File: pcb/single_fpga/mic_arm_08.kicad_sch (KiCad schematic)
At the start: 17 parts, among them U107 CDCLVC1108PW, U65 IM72D128V01XTMA1, U66 IM72D128V01XTMA1, U67 IM72D128V01XTMA1, U68 IM72D128V01XTMA1, U69 IM72D128V01XTMA1, U70 IM72D128V01XTMA1, U71 IM72D128V01XTMA1, U72 IM72D128V01XTMA1

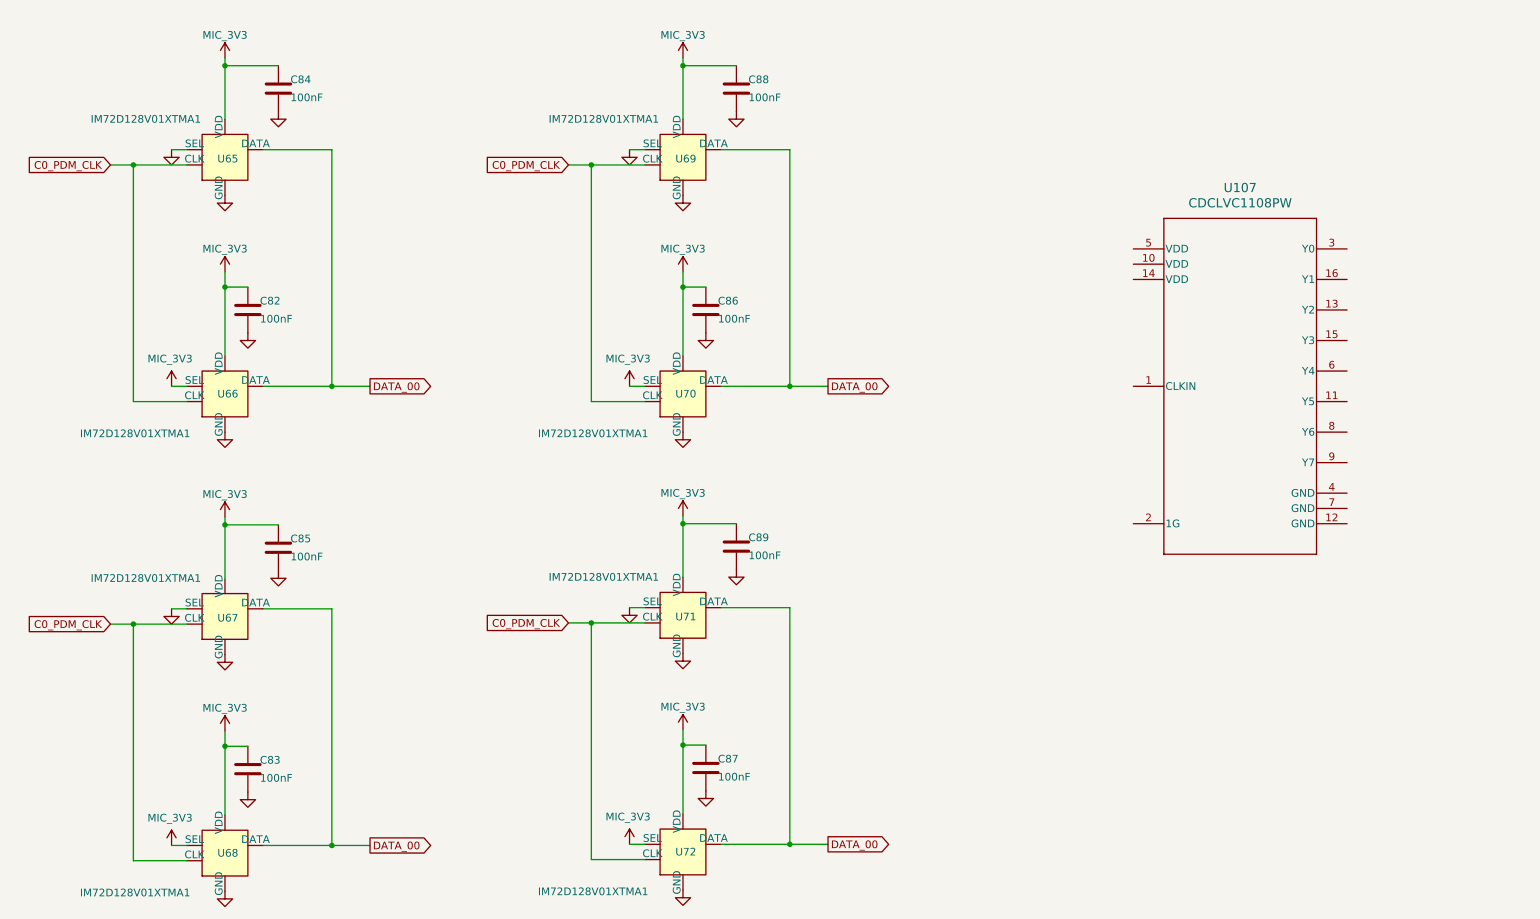
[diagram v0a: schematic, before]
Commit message: Fixed clocks and names.
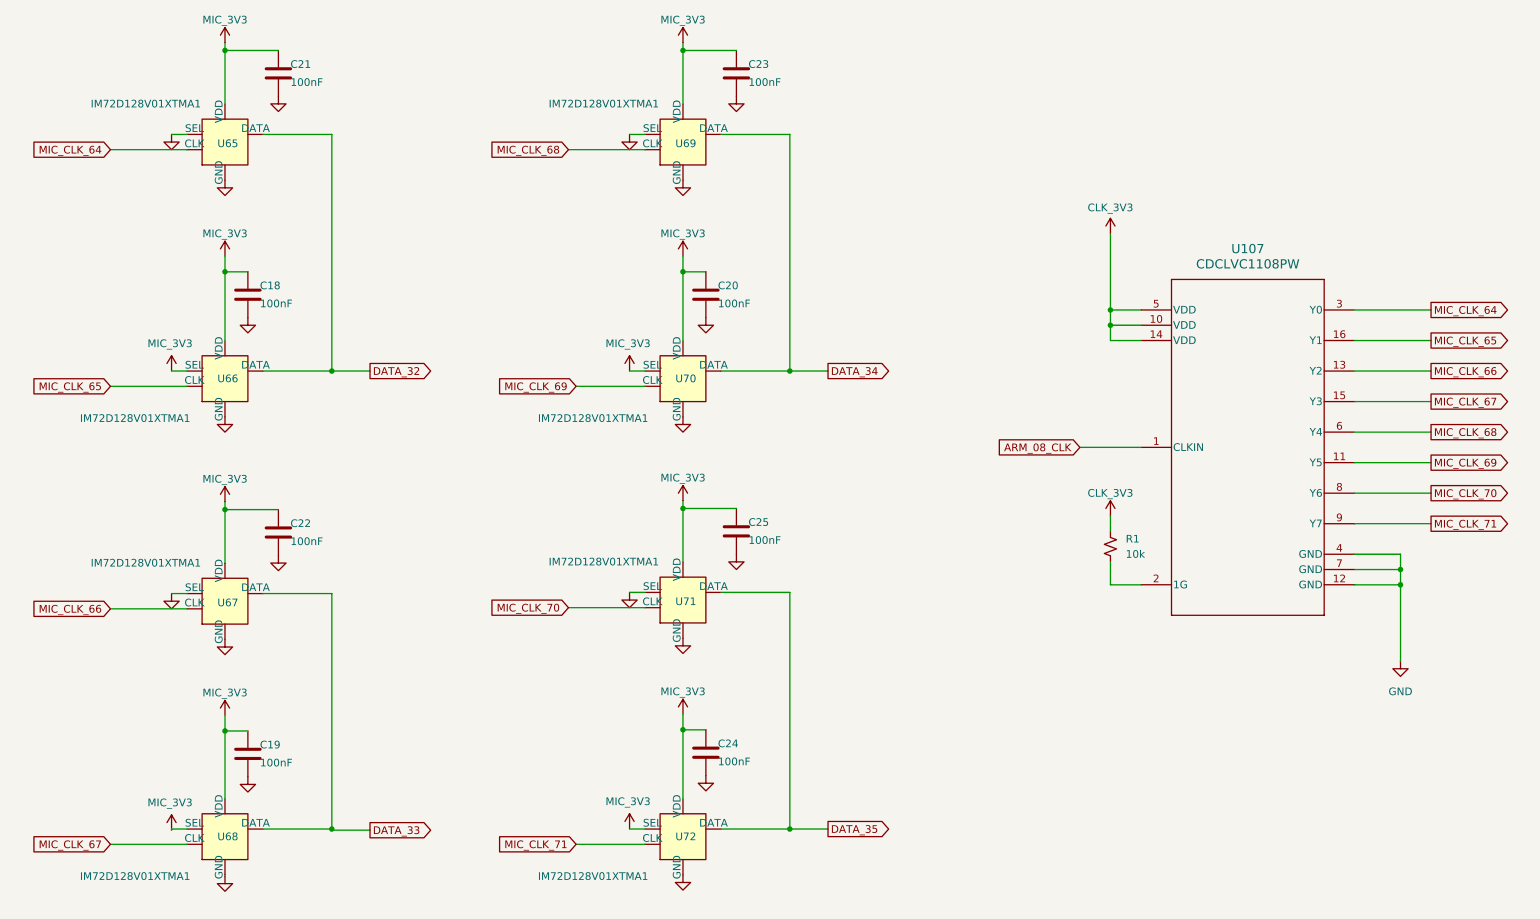
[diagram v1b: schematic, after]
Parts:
- removed C82, C83, C84, C85, C86, C87, C88, C89: 100nF, Capacitor_SMD:C_0603_1608Metric, symbol Device:C
- added C18, C19, C20, C21, C22, C23, C24, C25: 100nF, Capacitor_SMD:C_0603_1608Metric, symbol Device:C
- added R1: 10k, PCM_SparkFun-Resistor:R_0603_1608Metric, symbol PCM_SparkFun-Resistor:10k_0603
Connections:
- net GND: now also U107.12 (GND), U107.4 (GND), U107.7 (GND), C18.2, C19.2, C20.2, C21.2, C22.2, C23.2, C24.2, C25.2
- net MIC_3V3: now also C18.1, C19.1, C20.1, C21.1, C22.1, C23.1, C24.1, C25.1
- net ARM_08_CLK: now reaches U107.1 (CLKIN)
- net CLK_3V3: now reaches U107.10 (VDD)
- net CLK_3V3: now also U107.14 (VDD), U107.5 (VDD), R1.2
- net MIC_CLK_69: now reaches U107.11 (Y5)
- net MIC_CLK_69: now also U70.3 (CLK)
- net MIC_CLK_66: now reaches U107.13 (Y2)
- net MIC_CLK_66: now also U67.3 (CLK)
- net MIC_CLK_67: now reaches U107.15 (Y3)
- net MIC_CLK_67: now also U68.3 (CLK)
- net MIC_CLK_65: now reaches U107.16 (Y1)
- net MIC_CLK_65: now also U66.3 (CLK)
- net at U107.2 (1G): now also R1.1
- net MIC_CLK_64: now reaches U107.3 (Y0)
- net MIC_CLK_64: now also U65.3 (CLK)
- net MIC_CLK_68: now reaches U107.6 (Y4)
- net MIC_CLK_68: now also U69.3 (CLK)
- net MIC_CLK_70: now reaches U107.8 (Y6)
- net MIC_CLK_70: now also U71.3 (CLK)
- net MIC_CLK_71: now reaches U107.9 (Y7)
- net MIC_CLK_71: now also U72.3 (CLK)
- removed net C0_PDM_CLK: U65.3 (CLK), U66.3 (CLK), U67.3 (CLK), U68.3 (CLK), U69.3 (CLK), U70.3 (CLK), U71.3 (CLK), U72.3 (CLK)
- removed net DATA_00: U65.1 (DATA), U66.1 (DATA), U67.1 (DATA), U68.1 (DATA), U69.1 (DATA), U70.1 (DATA), U71.1 (DATA), U72.1 (DATA)
- new net DATA_32: U65.1 (DATA), U66.1 (DATA)
- new net DATA_33: U67.1 (DATA), U68.1 (DATA)
- new net DATA_34: U69.1 (DATA), U70.1 (DATA)
- new net DATA_35: U71.1 (DATA), U72.1 (DATA)

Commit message: Fixed all duplicate refdes's.
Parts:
- renumbered C18 to C82, C19 to C83, C20 to C84, C21 to C85, C22 to C86, C23 to C87, C24 to C88, C25 to C89, R1 to R13

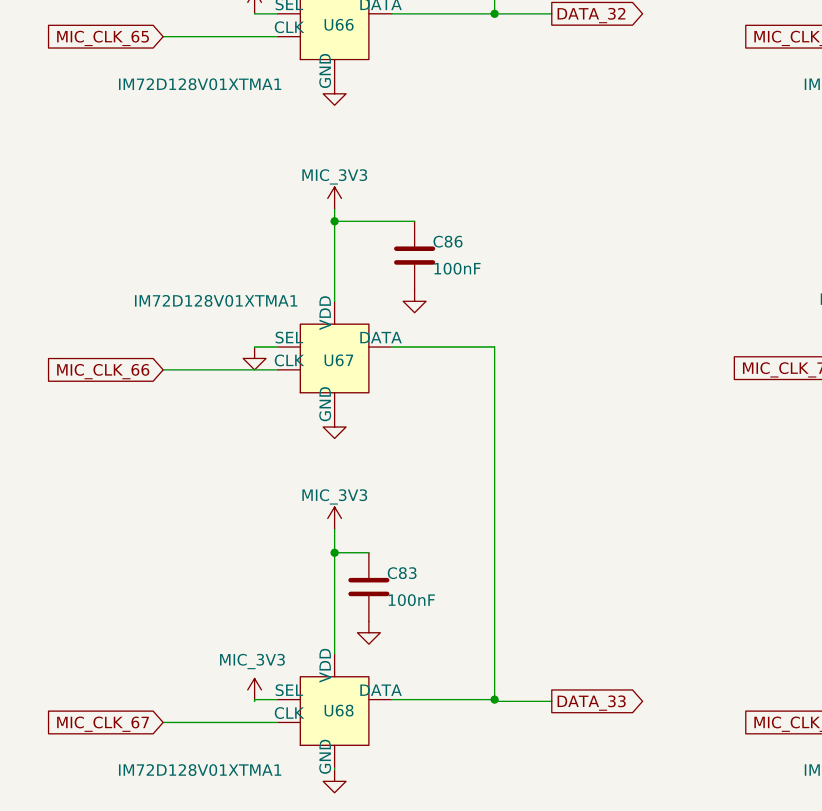
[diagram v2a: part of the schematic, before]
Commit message: Fixed symbol library references.
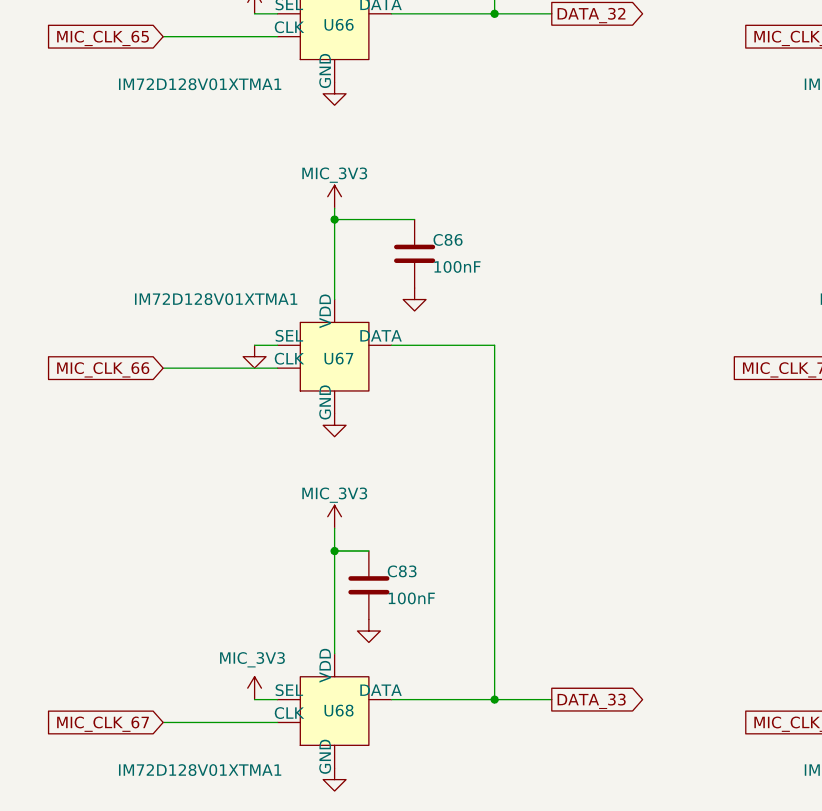
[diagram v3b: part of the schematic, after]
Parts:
- U107: footprint PW0016A_N -> CDCLVC1108:PW0016A_N

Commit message: Fixed footprints. Added missing mic. Relinked placed footprints.
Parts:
- U65, U66, U67, U68, U69, U70, U71, U72: footprint (none) -> IM72D128:IFX-PG-LLGA-5-4
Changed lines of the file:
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@@
 			)
 		)
-		(property "Footprint" ""
+		(property "Footprint" "IM72D128:IFX-PG-LLGA-5-4"
 			(at 59.69 160.02 0)
 			(hide yes)
@@
 			)
 		)
-		(property "Footprint" ""
+		(property "Footprint" "IM72D128:IFX-PG-LLGA-5-4"
 			(at 135.89 160.02 0)
 			(hide yes)
@@
 			)
 		)
-		(property "Footprint" ""
+		(property "Footprint" "IM72D128:IFX-PG-LLGA-5-4"
 			(at 59.69 83.82 0)
 			(hide yes)
@@
 			)
 		)
-		(property "Footprint" ""
+		(property "Footprint" "IM72D128:IFX-PG-LLGA-5-4"
 			(at 59.69 120.65 0)
 			(hide yes)
@@
 			)
 		)
-		(property "Footprint" ""
+		(property "Footprint" "IM72D128:IFX-PG-LLGA-5-4"
 			(at 59.69 44.45 0)
 			(hide yes)
@@
 			)
 		)
-		(property "Footprint" ""
+		(property "Footprint" "IM72D128:IFX-PG-LLGA-5-4"
 			(at 135.89 83.82 0)
 			(hide yes)
@@
 			)
 		)
-		(property "Footprint" ""
+		(property "Footprint" "IM72D128:IFX-PG-LLGA-5-4"
 			(at 135.89 44.45 0)
 			(hide yes)
@@
 			)
 		)
-		(property "Footprint" ""
+		(property "Footprint" "IM72D128:IFX-PG-LLGA-5-4"
 			(at 135.89 120.65 0)
 			(hide yes)

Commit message: Updated all refdes's.
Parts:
- removed C82, C83, C84, C85, C86, C87, C88, C89: 100nF, Capacitor_SMD:C_0603_1608Metric, symbol Device:C
- removed R13: 10k, PCM_SparkFun-Resistor:R_0603_1608Metric, symbol PCM_SparkFun-Resistor:10k_0603
- removed U107: CDCLVC1108PW, CDCLVC1108:PW0016A_N, symbol CDCLVC1108:CDCLVC1108PW
- removed U65, U66, U67, U68, U69, U70, U71, U72: IM72D128V01XTMA1, IM72D128:IFX-PG-LLGA-5-4, symbol multi_fpga:IM72D128
- added C65, C66, C67, C68, C69, C70, C71, C72: 100nF, Capacitor_SMD:C_0603_1608Metric, symbol Device:C
- added R9: 10k, PCM_SparkFun-Resistor:R_0603_1608Metric, symbol PCM_SparkFun-Resistor:10k_0603
- added U73, U74, U75, U76, U77, U78, U79, U80: IM72D128V01XTMA1, IM72D128:IFX-PG-LLGA-5-4, symbol multi_fpga:IM72D128
- added U81: CDCLVC1108PW, CDCLVC1108:PW0016A_N, symbol CDCLVC1108:CDCLVC1108PW
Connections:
- net ARM_08_CLK: now also U81.1 (CLKIN)
- net CLK_3V3: now also R9.2, U81.10 (VDD), U81.14 (VDD), U81.5 (VDD)
- net DATA_32: now also U73.1 (DATA), U74.1 (DATA)
- net DATA_33: now also U75.1 (DATA), U76.1 (DATA)
- net DATA_34: now also U77.1 (DATA), U78.1 (DATA)
- net DATA_35: now also U79.1 (DATA), U80.1 (DATA)
- net GND: now also C65.2, C66.2, C67.2, C68.2, C69.2, C70.2, C71.2, C72.2, U73.4 (SEL), U73.5 (GND), U74.5 (GND), U75.4 (SEL), U75.5 (GND), U76.5 (GND), U77.4 (SEL), U77.5 (GND), U78.5 (GND), U79.4 (SEL), U79.5 (GND), U80.5 (GND), U81.12 (GND), U81.4 (GND), U81.7 (GND)
- net MIC_3V3: now also C65.1, C66.1, C67.1, C68.1, C69.1, C70.1, C71.1, C72.1, U73.2 (VDD), U74.2 (VDD), U74.4 (SEL), U75.2 (VDD), U76.2 (VDD), U76.4 (SEL), U77.2 (VDD), U78.2 (VDD), U78.4 (SEL), U79.2 (VDD), U80.2 (VDD), U80.4 (SEL)
- net MIC_CLK_64: now also U73.3 (CLK), U81.3 (Y0)
- net MIC_CLK_65: now also U74.3 (CLK), U81.16 (Y1)
- net MIC_CLK_66: now also U75.3 (CLK), U81.13 (Y2)
- net MIC_CLK_67: now also U76.3 (CLK), U81.15 (Y3)
- net MIC_CLK_68: now also U77.3 (CLK), U81.6 (Y4)
- net MIC_CLK_69: now also U78.3 (CLK), U81.11 (Y5)
- net MIC_CLK_70: now also U79.3 (CLK), U81.8 (Y6)
- net MIC_CLK_71: now also U80.3 (CLK), U81.9 (Y7)
- new net: R9.1, U81.2 (1G)
